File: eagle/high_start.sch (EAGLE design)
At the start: 32 parts, among them Q1 16Mhz, Q2 IRF510, Q3 IRF510, Q4 IRF510, U2 ATMEGA328P_PDIP, X1 22-23-2041, X2 22-23-2041, X3 22-23-2041, X4 22-23-2041

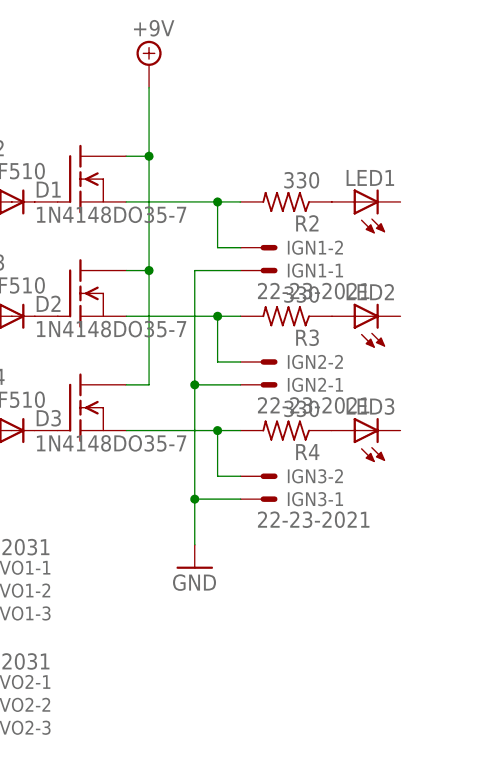
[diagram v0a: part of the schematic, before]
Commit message: tied led cathodes to gnd
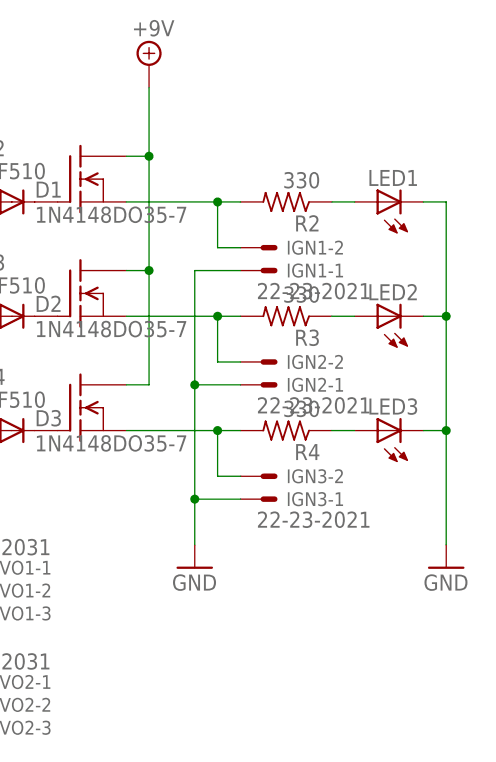
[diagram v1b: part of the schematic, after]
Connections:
- net GND: now also LED1.C, LED2.C, LED3.C
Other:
- moved on the sheet: LED1, LED2, LED3
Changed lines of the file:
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@@
 <part name="LED3" library="led" deviceset="LED" device="5MM"/>
 <part name="GND5" library="supply1" deviceset="GND" device=""/>
+<part name="GND6" library="supply1" deviceset="GND" device=""/>
 </parts>
 <sheets>
@@
 <instance part="IGN3" gate="-1" x="129.54" y="58.42" rot="MR180"/>
 <instance part="IGN3" gate="-2" x="129.54" y="60.96" rot="MR180"/>
-<instance part="LED1" gate="G$1" x="139.7" y="91.44" rot="R90"/>
-<instance part="LED2" gate="G$1" x="139.7" y="78.74" rot="R90"/>
-<instance part="LED3" gate="G$1" x="139.7" y="66.04" rot="R90"/>
+<instance part="LED1" gate="G$1" x="142.24" y="91.44" rot="R90"/>
+<instance part="LED2" gate="G$1" x="142.24" y="78.74" rot="R90"/>
+<instance part="LED3" gate="G$1" x="142.24" y="66.04" rot="R90"/>
 <instance part="GND5" gate="1" x="121.92" y="50.8"/>
+<instance part="GND6" gate="1" x="149.86" y="50.8"/>
 </instances>
 <busses>
@@
 <junction x="121.92" y="71.12"/>
 </segment>
+<segment>
+<pinref part="LED1" gate="G$1" pin="C"/>
+<pinref part="GND6" gate="1" pin="GND"/>
+<wire x1="147.32" y1="91.44" x2="149.86" y2="91.44" width="0.1524" layer="91"/>
+<wire x1="149.86" y1="91.44" x2="149.86" y2="78.74" width="0.1524" layer="91"/>
+<pinref part="LED3" gate="G$1" pin="C"/>
+<wire x1="149.86" y1="78.74" x2="149.86" y2="66.04" width="0.1524" layer="91"/>
+<wire x1="149.86" y1="66.04" x2="149.86" y2="53.34" width="0.1524" layer="91"/>
+<wire x1="147.32" y1="66.04" x2="149.86" y2="66.04" width="0.1524" layer="91"/>
+<junction x="149.86" y="66.04"/>
+<pinref part="LED2" gate="G$1" pin="C"/>
+<wire x1="147.32" y1="78.74" x2="149.86" y2="78.74" width="0.1524" layer="91"/>
+<junction x="149.86" y="78.74"/>
+</segment>
 </net>
 <net name="N$1" class="0">
@@
 <pinref part="R2" gate="G$1" pin="1"/>
 <pinref part="LED1" gate="G$1" pin="A"/>
+<wire x1="139.7" y1="91.44" x2="137.16" y2="91.44" width="0.1524" layer="91"/>
 </segment>
 </net>
@@
 <pinref part="R3" gate="G$1" pin="1"/>
 <pinref part="LED2" gate="G$1" pin="A"/>
+<wire x1="139.7" y1="78.74" x2="137.16" y2="78.74" width="0.1524" layer="91"/>
 </segment>
 </net>
@@
 <pinref part="R4" gate="G$1" pin="1"/>
 <pinref part="LED3" gate="G$1" pin="A"/>
-</segment>
-</net>
+<wire x1="139.7" y1="66.04" x2="137.16" y2="66.04" width="0.1524" layer="91"/>
+</segment>
+</net>

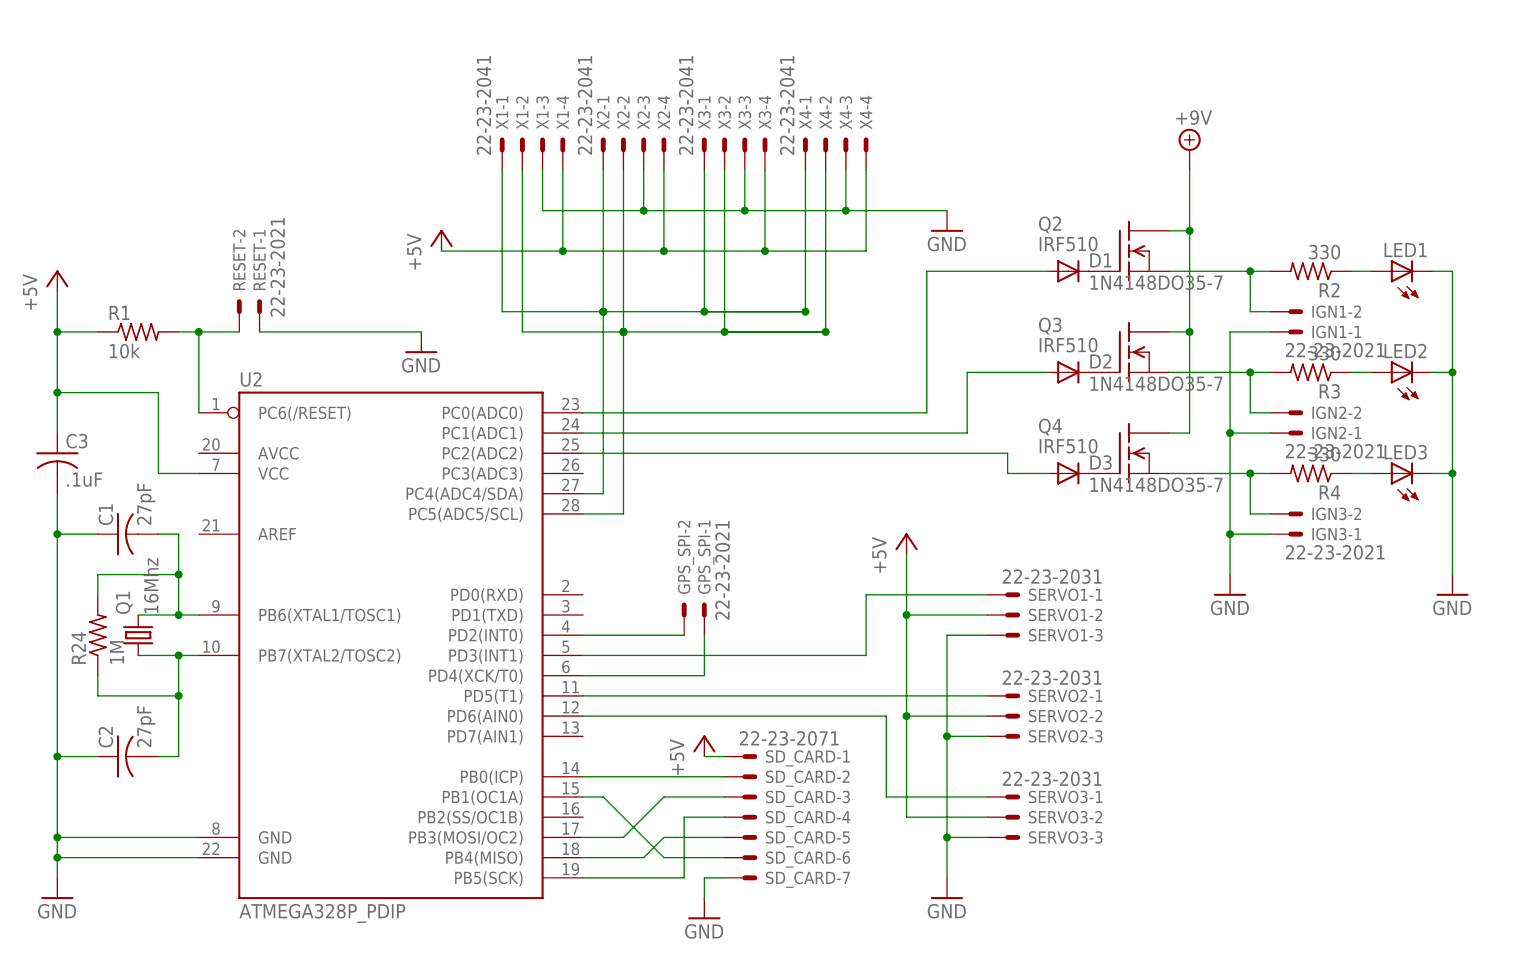
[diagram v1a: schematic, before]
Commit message: added battery and reg and layed out board
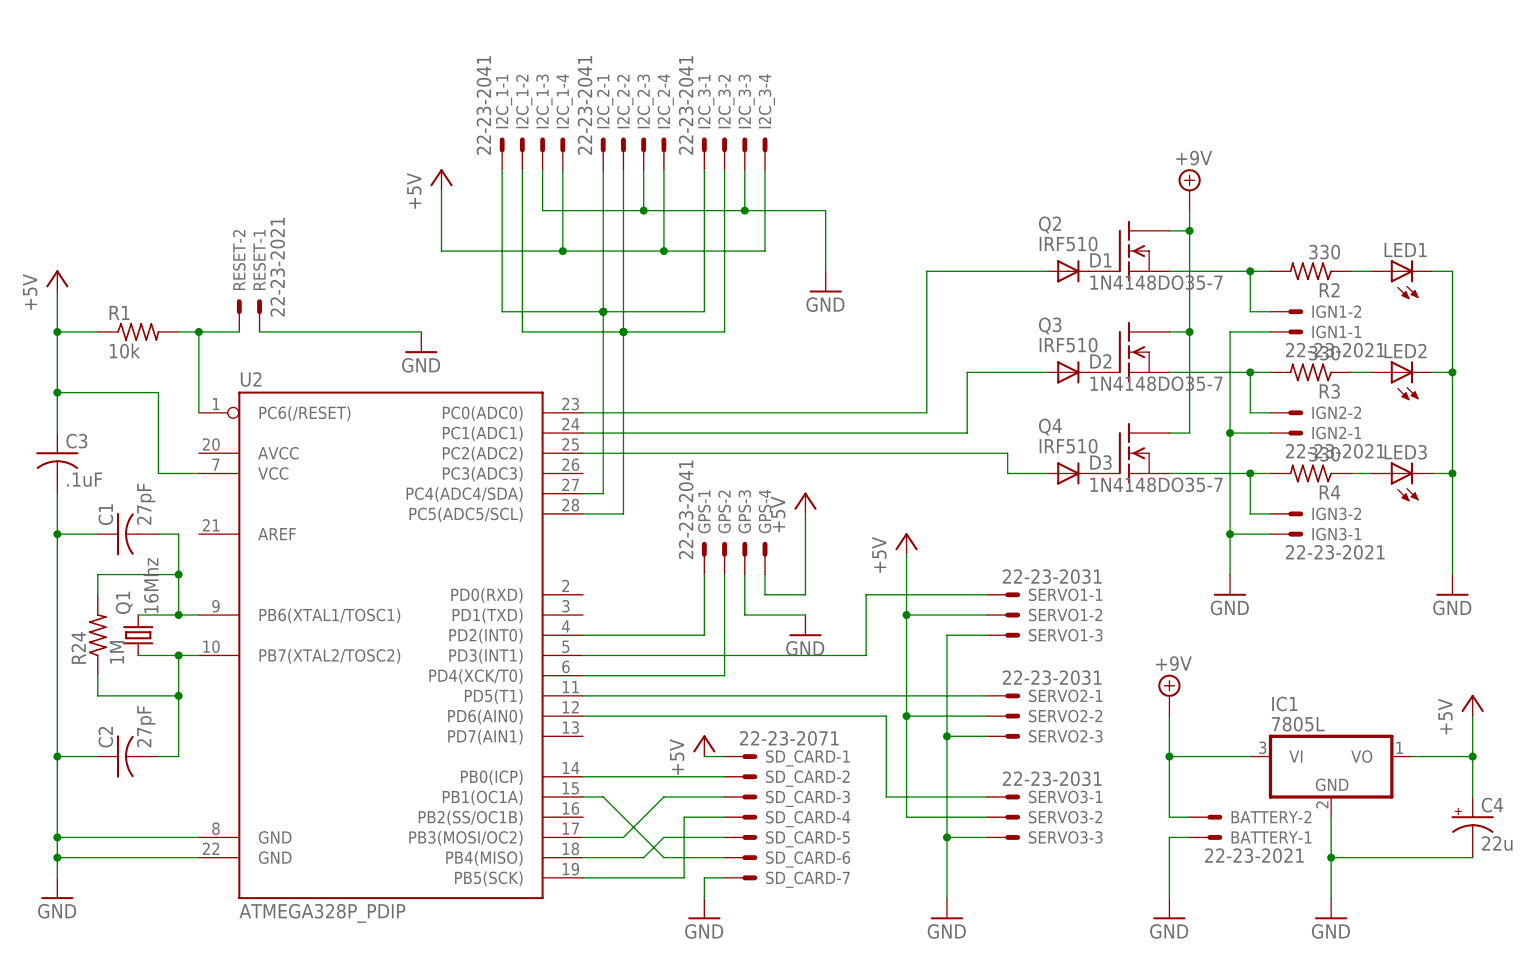
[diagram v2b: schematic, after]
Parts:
- removed GPS_SPI: 22-23-2021, con-molex:22-23-2021
- removed X4: 22-23-2041, con-molex:22-23-2041
- added BATTERY: 22-23-2021, con-molex:22-23-2021
- added C4: 22u, rcl:CPOL-USB45181A
- added GPS: 22-23-2041, con-molex:22-23-2041
- added IC1: 7805L, linear:7805L
- renumbered X1 to I2C_1, X2 to I2C_2, X3 to I2C_3
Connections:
- net +5V: now also C4.+, GPS-4.S, IC1.VO; no longer X4-4.S
- net +9V: now also BATTERY-2.S, IC1.VI
- net GND: now also BATTERY-1.S, C4.-, GPS-3.S, IC1.GND; no longer X4-3.S
- net N$1: no longer X4-2.S
- net N$2: no longer X4-1.S
- net N$3: now also GPS-1.S; no longer GPS_SPI-2.S
- net N$6: now also GPS-2.S; no longer GPS_SPI-1.S

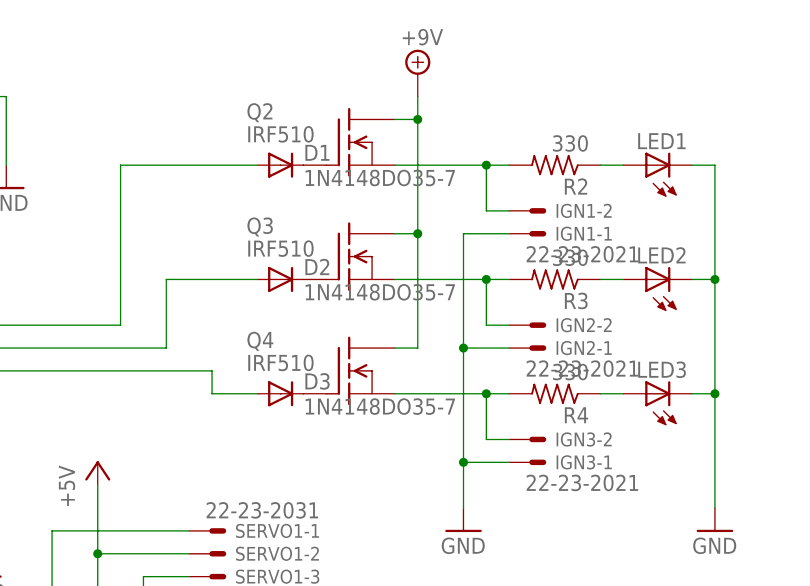
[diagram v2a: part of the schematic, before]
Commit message: moved power connector between fets and micro
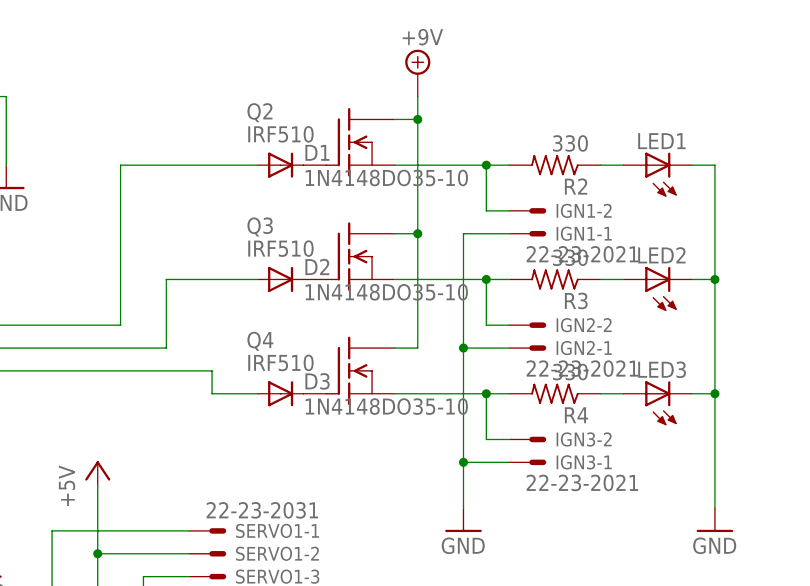
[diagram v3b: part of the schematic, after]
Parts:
- D1, D2, D3: value 1N4148DO35-7 -> 1N4148DO35-10; device diode:1N4148DO35-7 -> diode:1N4148DO35-10
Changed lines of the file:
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@@
 <grid distance="0.1" unitdist="inch" unit="inch" style="lines" multiple="1" display="no" altdistance="0.01" altunitdist="inch" altunit="inch"/>
 <layers>
-<layer number="1" name="Top" color="4" fill="1" visible="no" active="no"/>
-<layer number="16" name="Bottom" color="1" fill="1" visible="no" active="no"/>
-<layer number="17" name="Pads" color="2" fill="1" visible="no" active="no"/>
-<layer number="18" name="Vias" color="2" fill="1" visible="no" active="no"/>
-<layer number="19" name="Unrouted" color="6" fill="1" visible="no" active="no"/>
-<layer number="20" name="Dimension" color="15" fill="1" visible="no" active="no"/>
-<layer number="21" name="tPlace" color="7" fill="1" visible="no" active="no"/>
-<layer number="22" name="bPlace" color="7" fill="1" visible="no" active="no"/>
-<layer number="23" name="tOrigins" color="15" fill="1" visible="no" active="no"/>
-<layer number="24" name="bOrigins" color="15" fill="1" visible="no" active="no"/>
-<layer number="25" name="tNames" color="7" fill="1" visible="no" active="no"/>
-<layer number="26" name="bNames" color="7" fill="1" visible="no" active="no"/>
-<layer number="27" name="tValues" color="7" fill="1" visible="no" active="no"/>
-<layer number="28" name="bValues" color="7" fill="1" visible="no" active="no"/>
+<layer number="1" name="Top" color="4" fill="1" visible="yes" active="no"/>
+<layer number="16" name="Bottom" color="1" fill="1" visible="yes" active="no"/>
+<layer number="17" name="Pads" color="2" fill="1" visible="yes" active="no"/>
+<layer number="18" name="Vias" color="2" fill="1" visible="yes" active="no"/>
+<layer number="19" name="Unrouted" color="6" fill="1" visible="yes" active="no"/>
+<layer number="20" name="Dimension" color="15" fill="1" visible="yes" active="no"/>
+<layer number="21" name="tPlace" color="7" fill="1" visible="yes" active="no"/>
+<layer number="22" name="bPlace" color="7" fill="1" visible="yes" active="no"/>
+<layer number="23" name="tOrigins" color="15" fill="1" visible="yes" active="no"/>
+<layer number="24" name="bOrigins" color="15" fill="1" visible="yes" active="no"/>
+<layer number="25" name="tNames" color="7" fill="1" visible="yes" active="no"/>
+<layer number="26" name="bNames" color="7" fill="1" visible="yes" active="no"/>
+<layer number="27" name="tValues" color="7" fill="1" visible="yes" active="no"/>
+<layer number="28" name="bValues" color="7" fill="1" visible="yes" active="no"/>
 <layer number="29" name="tStop" color="7" fill="3" visible="no" active="no"/>
 <layer number="30" name="bStop" color="7" fill="6" visible="no" active="no"/>
@@
 <layer number="35" name="tGlue" color="7" fill="4" visible="no" active="no"/>
 <layer number="36" name="bGlue" color="7" fill="5" visible="no" active="no"/>
-<layer number="37" name="tTest" color="7" fill="1" visible="no" active="no"/>
-<layer number="38" name="bTest" color="7" fill="1" visible="no" active="no"/>
+<layer number="37" name="tTest" color="7" fill="1" visible="yes" active="no"/>
+<layer number="38" name="bTest" color="7" fill="1" visible="yes" active="no"/>
 <layer number="39" name="tKeepout" color="4" fill="11" visible="no" active="no"/>
 <layer number="40" name="bKeepout" color="1" fill="11" visible="no" active="no"/>
@@
 <layer number="44" name="Drills" color="7" fill="1" visible="no" active="no"/>
 <layer number="45" name="Holes" color="7" fill="1" visible="no" active="no"/>
-<layer number="46" name="Milling" color="3" fill="1" visible="no" active="no"/>
-<layer number="47" name="Measures" color="7" fill="1" visible="no" active="no"/>
-<layer number="48" name="Document" color="7" fill="1" visible="no" active="no"/>
-<layer number="49" name="Reference" color="7" fill="1" visible="no" active="no"/>
-<layer number="50" name="dxf" color="7" fill="1" visible="no" active="no"/>
-<layer number="51" name="tDocu" color="7" fill="1" visible="no" active="no"/>
-<layer number="52" name="bDocu" color="7" fill="1" visible="no" active="no"/>
-<layer number="53" name="tGND_GNDA" color="7" fill="9" visible="no" active="no"/>
-<layer number="54" name="bGND_GNDA" color="1" fill="9" visible="no" active="no"/>
-<layer number="56" name="wert" color="7" fill="1" visible="no" active="no"/>
-<layer number="57" name="tCAD" color="7" fill="1" visible="no" active="no"/>
-<layer number="59" name="tCarbon" color="7" fill="1" visible="no" active="no"/>
-<layer number="60" name="bCarbon" color="7" fill="1" visible="no" active="no"/>
+<layer number="46" name="Milling" color="3" fill="1" visible="yes" active="no"/>
+<layer number="47" name="Measures" color="7" fill="1" visible="yes" active="no"/>
+<layer number="48" name="Document" color="7" fill="1" visible="yes" active="no"/>
+<layer number="49" name="Reference" color="7" fill="1" visible="yes" active="no"/>
+<layer number="50" name="dxf" color="7" fill="1" visible="yes" active="no"/>
+<layer number="51" name="tDocu" color="7" fill="1" visible="yes" active="no"/>
+<layer number="52" name="bDocu" color="7" fill="1" visible="yes" active="no"/>
+<layer number="53" name="tGND_GNDA" color="7" fill="9" visible="yes" active="no"/>
+<layer number="54" name="bGND_GNDA" color="1" fill="9" visible="yes" active="no"/>
+<layer number="56" name="wert" color="7" fill="1" visible="yes" active="no"/>
+<layer number="57" name="tCAD" color="7" fill="1" visible="yes" active="no"/>
+<layer number="59" name="tCarbon" color="7" fill="1" visible="yes" active="no"/>
+<layer number="60" name="bCarbon" color="7" fill="1" visible="yes" active="no"/>
 <layer number="90" name="Modules" color="5" fill="1" visible="yes" active="yes"/>
 <layer number="91" name="Nets" color="2" fill="1" visible="yes" active="yes"/>
@@
 <part name="Q3" library="transistor-fet" deviceset="IRF510" device=""/>
 <part name="SUPPLY1" library="supply2" deviceset="+9V" device=""/>
-<part name="D1" library="diode" deviceset="1N4148" device="DO35-7"/>
-<part name="D2" library="diode" deviceset="1N4148" device="DO35-7"/>
+<part name="D1" library="diode" deviceset="1N4148" device="DO35-10" value="1N4148DO35-10"/>
+<part name="D2" library="diode" deviceset="1N4148" device="DO35-10" value="1N4148DO35-10"/>
 <part name="Q4" library="transistor-fet" deviceset="IRF510" device=""/>
-<part name="D3" library="diode" deviceset="1N4148" device="DO35-7"/>
+<part name="D3" library="diode" deviceset="1N4148" device="DO35-10" value="1N4148DO35-10"/>
 <part name="SERVO1" library="con-molex" deviceset="22-23-2031" device=""/>
 <part name="SERVO2" library="con-molex" deviceset="22-23-2031" device=""/>

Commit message: routed
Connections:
- net +5V: now also U2.AREF
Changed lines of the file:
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@@
 <wire x1="-25.4" y1="71.12" x2="-25.4" y2="76.2" width="0.1524" layer="91"/>
 <junction x="-25.4" y="76.2"/>
+<pinref part="U2" gate="G$1" pin="AREF"/>
+<wire x1="-7.62" y1="58.42" x2="-7.62" y2="63.5" width="0.1524" layer="91"/>
+<wire x1="-7.62" y1="63.5" x2="-12.7" y2="63.5" width="0.1524" layer="91"/>
+<wire x1="-12.7" y1="63.5" x2="-12.7" y2="66.04" width="0.1524" layer="91"/>
+<junction x="-12.7" y="66.04"/>
 </segment>
 <segment>
